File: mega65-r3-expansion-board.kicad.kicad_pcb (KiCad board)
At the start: 4 copper layers, 215 x 126.9 mm, 115 parts, among them J1 Conn_01x04, J10 PMOD2, J11 Conn_02x05_Odd_Even, J12 Conn_02x17_Odd_Even, J13 Conn_02x17_Odd_Even, J14 Component A/V, J15 ESP32 Connector, J16 MD-90SM, J17 Conn_01x03, J18 Conn_01x02, J19 Conn_01x03, J2 Conn_01x04, J20 Conn_01x02, J21 Conn_01x03, J3 C64_User_Port, J4 Conn_01x02, J5 C64_Tape_Port, J6 OKR-T/3-W12-C, J7 Conn_02x06_Odd_Even, J8 Conn_02x06_Odd_Even, J9 PMOD1, U1 74HC595, U10 74LS125, U11 74HC595, U12 74LS125, U13 74LS125, U2 74LVC165, U3 74LS125, U4 74HC595, U5 74LVC165, U6 74HC595, U7 74LVC165, U8 74LS125, U9 74LS125

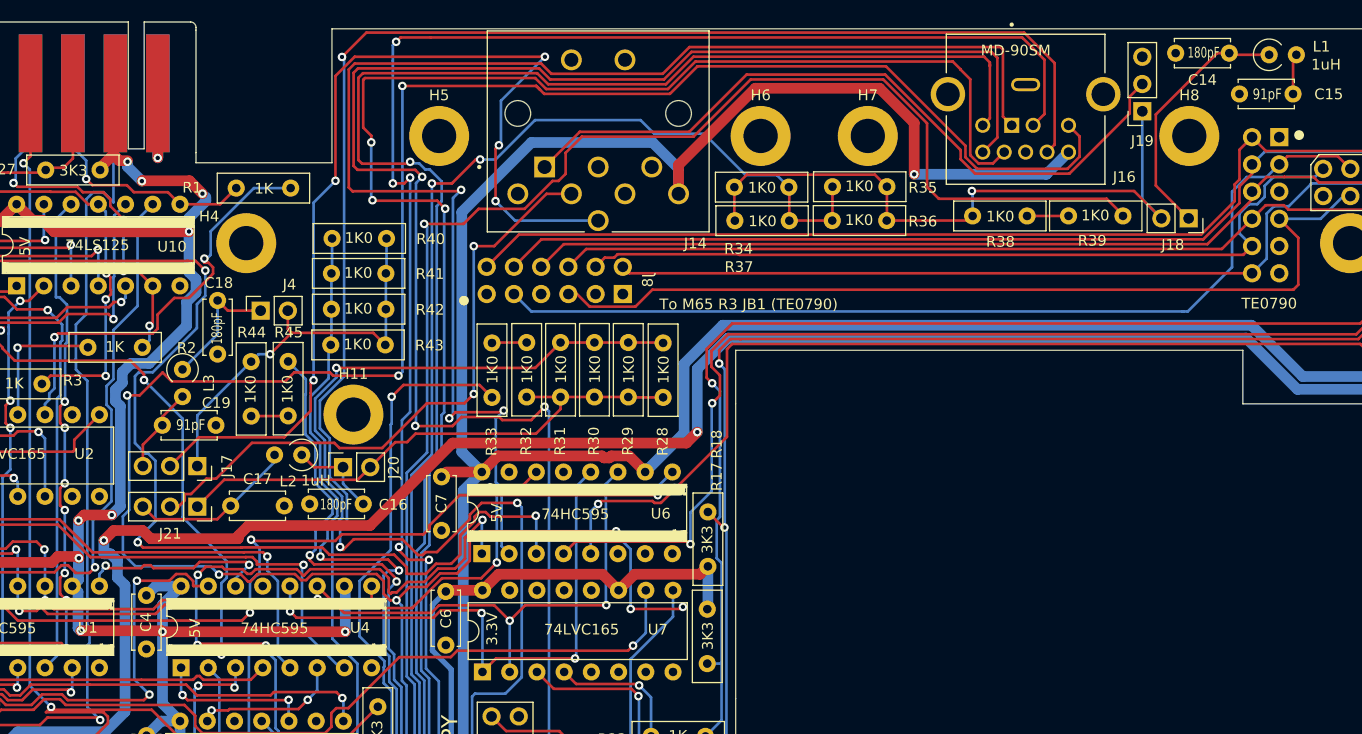
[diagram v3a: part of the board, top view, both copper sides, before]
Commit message: video filter routing and DRC good
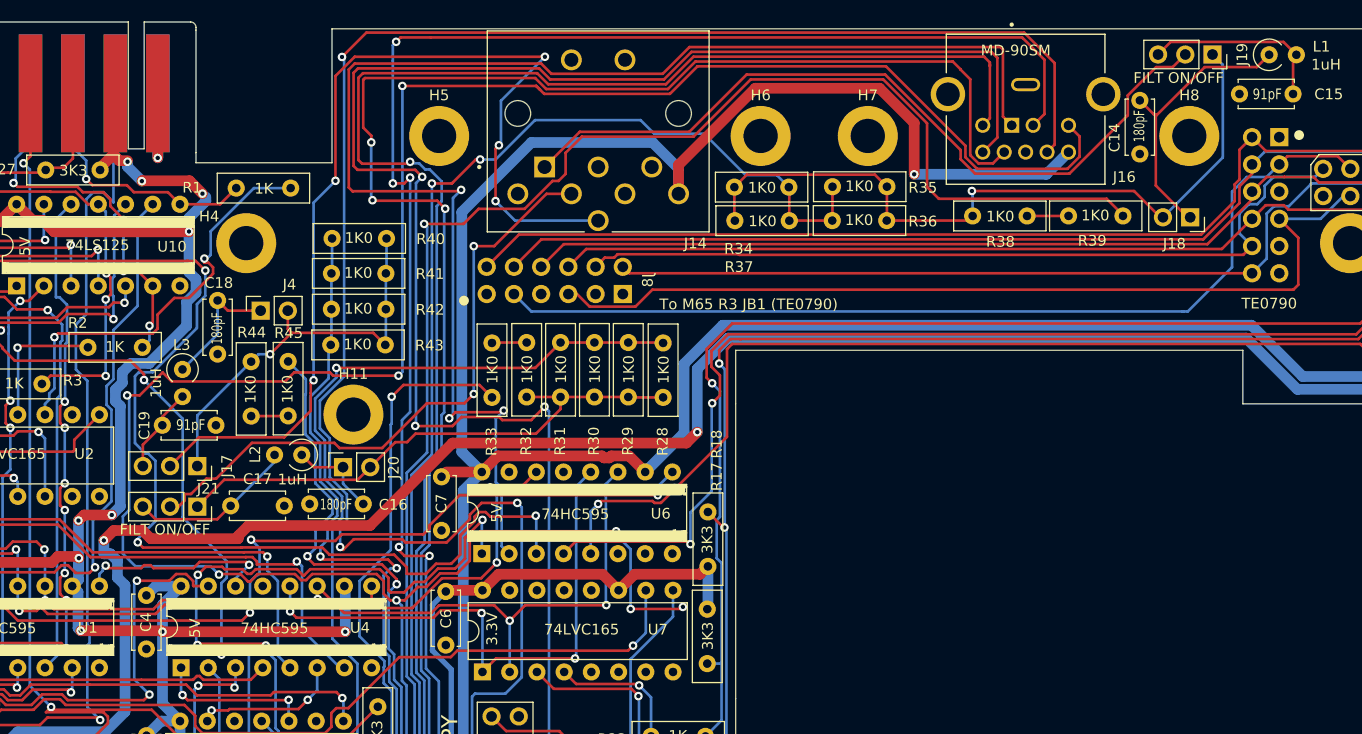
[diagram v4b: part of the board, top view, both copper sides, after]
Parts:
- moved C14 9.44 mm to (169.2, 34.4), turned to -90 degrees
- moved J19 8.42 mm to (176.0, 30.1), turned to -90 degrees
- moved J18 0.18 mm to (173.9, 45.3)
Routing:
- net /Composite and component video output/COMPOSITE_FILTERED: track 3.79 -> 17.7 mm
- net /Composite and component video output/COMPOSITE_UNFILTERED: track 61.5 -> 68.7 mm
- net /Composite and component video output/COMPOSITE_OUT: track 68.1 -> 73.4 mm
- net Net-(J18-Pin_1): track 24.0 -> 25.9 mm
- net /C1565 External C65 Drive Port/CLOCK_5V: track 218.8 -> 217.8 mm
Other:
- board text added: "FILT ON/OFF"
